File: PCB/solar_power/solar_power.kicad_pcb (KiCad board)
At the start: 2 copper layers, 50 x 50 mm, 16 parts, among them U1 BQ25570

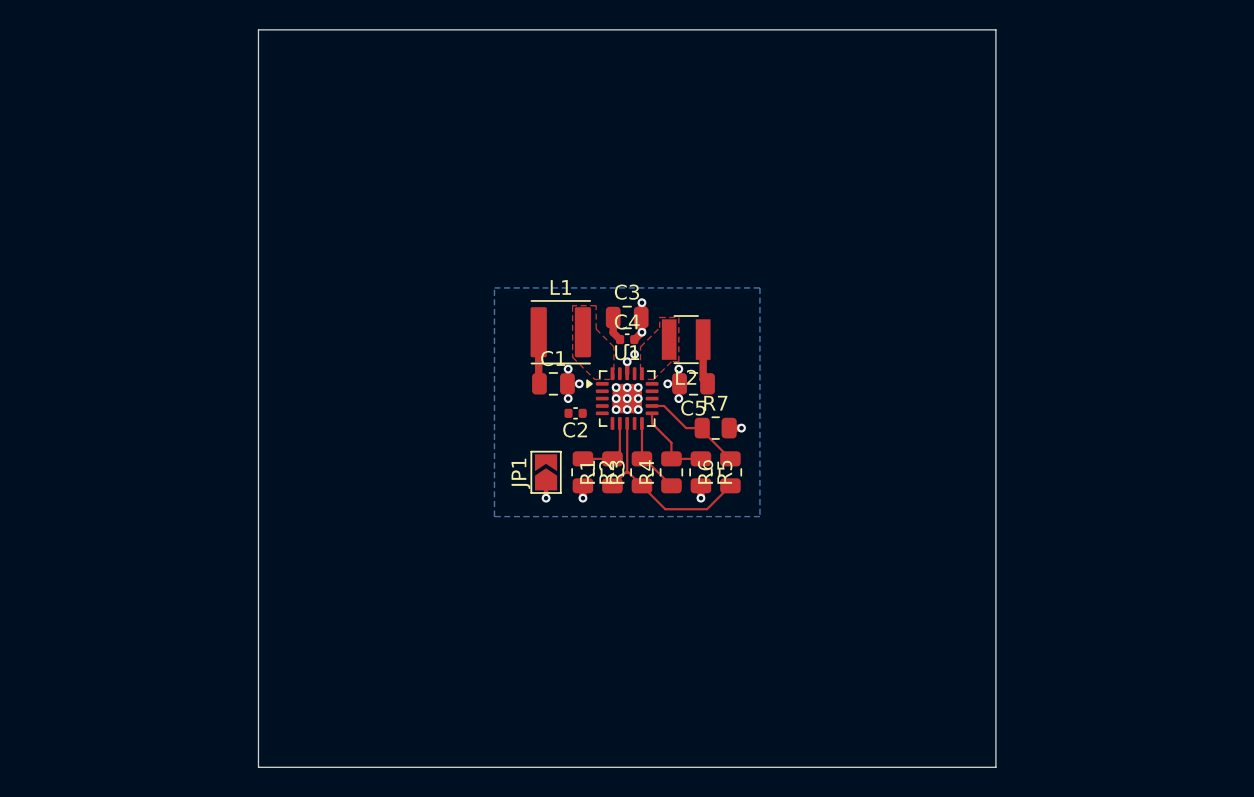
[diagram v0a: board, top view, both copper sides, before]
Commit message: Added 18650 battery holder to library and solar PCB
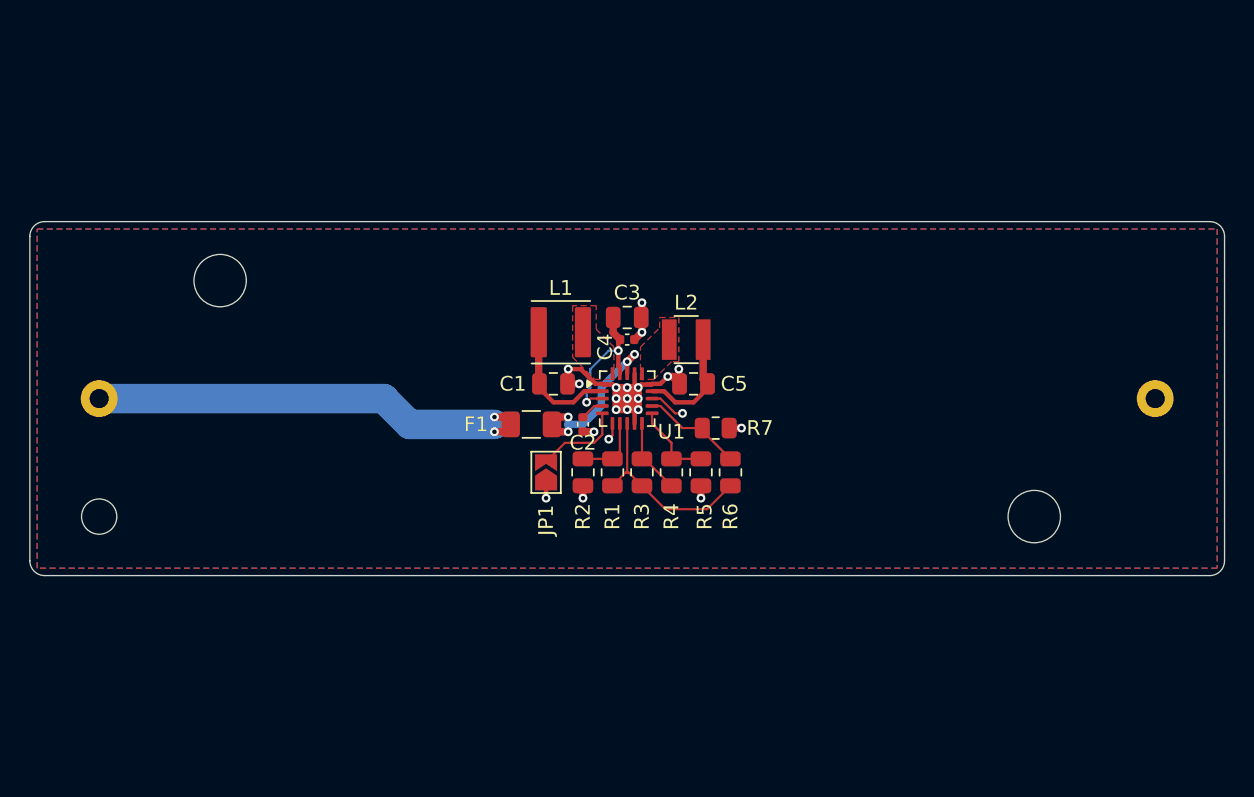
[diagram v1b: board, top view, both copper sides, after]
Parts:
- added BT1: 18650, DWlib:Keystone_1043P_1x18650, B.Cu at (125.0, 75.0)
- added F1: 200mA, Fuse:Fuse_1206_3216Metric, F.Cu at (118.5, 76.8)
- moved C2 0.90 mm to (122.0, 76.8), turned to -90 degrees
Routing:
- net Net-(BT1-+): track 0.00 -> 30.1 mm, vias 0 -> 2
- net GND: track 6.26 -> 20.7 mm, vias 21 -> 20
- net /VBAT: track 0.81 -> 11.6 mm, vias 2 -> 4
- net /VSTOR: track 1.69 -> 10.0 mm, vias 0 -> 2
- net Net-(JP1-B): track 0.00 -> 6.01 mm
- net /SOLAR_IN: track 3.52 -> 8.79 mm
- net /VOUT: track 3.12 -> 7.89 mm
- net unconnected-(U1-VBAT_OK-Pad13): track 0.00 -> 2.48 mm, vias 0 -> 1
- net Net-(U1-VREF_SAMP): track 0.00 -> 1.63 mm
- net unconnected-(U1-VOUT_EN-Pad6): track 0.00 -> 1.17 mm, vias 0 -> 1
- added copper zone on F.Cu, net GND
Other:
- board size 50 x 50 mm -> 81 x 24 mm

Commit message: Added filtering and connectors to solar PCB with 3D models
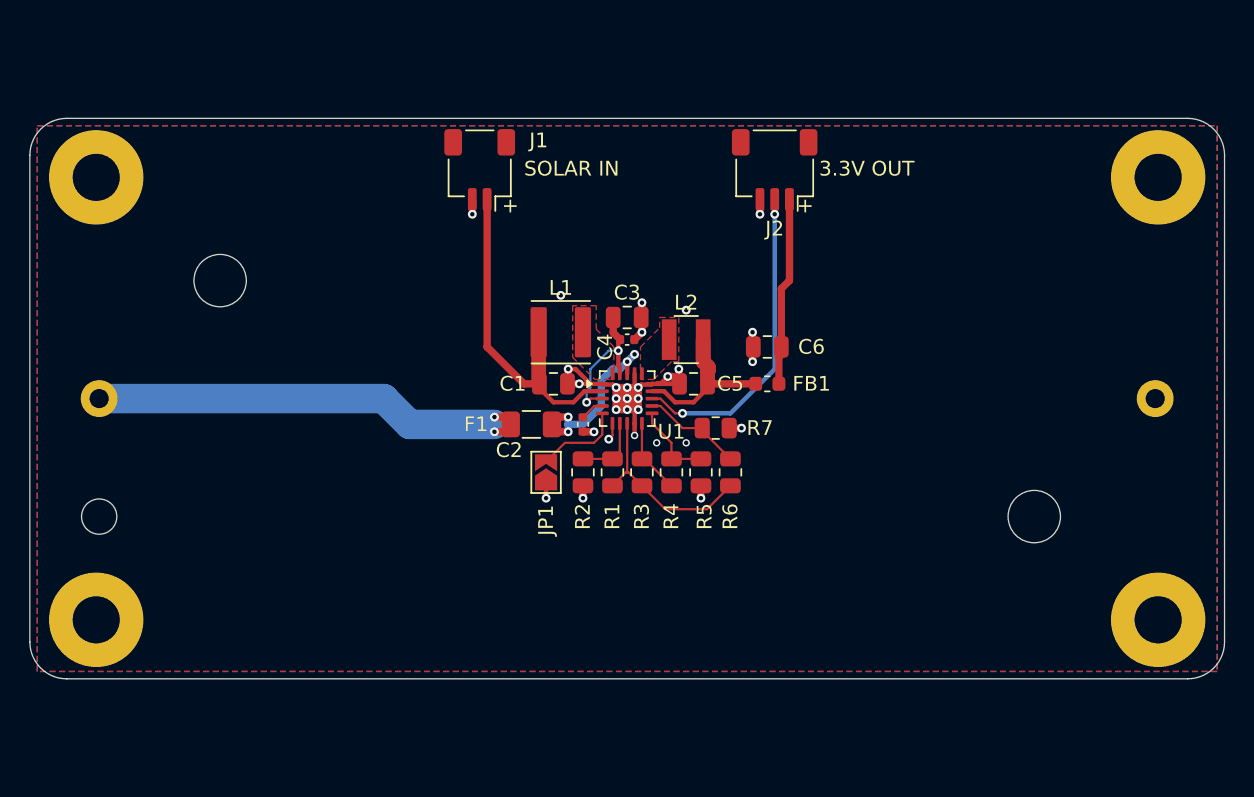
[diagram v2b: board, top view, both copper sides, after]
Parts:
- added C6: 22u, Capacitor_SMD:C_0805_2012Metric, F.Cu at (134.5, 71.5)
- added FB1: 600R, Inductor_SMD:L_0603_1608Metric, F.Cu at (134.5, 74.0)
- added H1: M3, MountingHole:MountingHole_3.2mm_M3_Pad, F.Cu at (89.0, 60.0)
- added H2: M3, MountingHole:MountingHole_3.2mm_M3_Pad, F.Cu at (161.0, 60.0)
- added H3: M3, MountingHole:MountingHole_3.2mm_M3_Pad, F.Cu at (89.0, 90.0)
- added H4: M3, MountingHole:MountingHole_3.2mm_M3_Pad, F.Cu at (161.0, 90.0)
- added J1: SH_SM02B, Connector_JST:JST_SH_SM02B-SRSS-TB_1x02-1MP_P1.00mm_Horizontal, F.Cu at (115.0, 59.5)
- added J2: SH_SM03B, Connector_JST:JST_SH_SM03B-SRSS-TB_1x03-1MP_P1.00mm_Horizontal, F.Cu at (135.0, 59.5)
- C4: value 10n -> 0.1u
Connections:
- net /VOUT renamed Net-(U1-VOUT)
- U1 pad 13: unconnected-(U1-VBAT_OK-Pad13) -> /VBAT_OK
- U1 pad 6: unconnected-(U1-VOUT_EN-Pad6) -> /VOUT_EN
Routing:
- net /VBAT_OK: track 0.00 -> 21.5 mm, vias 0 -> 2
- net /SOLAR_IN: track 8.79 -> 23.4 mm
- net /VOUT: track 0.00 -> 12.8 mm
- net GND: track 20.7 -> 29.4 mm, vias 20 -> 29
- net Net-(U1-VOUT): track 7.89 -> 11.2 mm
- net unconnected-(U1-VBAT_OK-Pad13): track 2.48 -> 0.00 mm, vias 1 -> 0
- net unconnected-(U1-VOUT_EN-Pad6): track 1.17 -> 0.00 mm, vias 1 -> 0
- net /VOUT_EN: track 0.00 -> 1.17 mm, vias 0 -> 1
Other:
- board size 81 x 24 mm -> 81 x 38 mm
- board text added: "+"
- board text added: "3.3V OUT"
- board text added: "SOLAR IN"
